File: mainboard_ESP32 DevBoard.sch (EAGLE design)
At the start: 41 parts, among them IC1 OP-AMP-2-LONG, IC2 OP-AMP-2-LONG, IC3 74HC08N, K1 AQH213, X1 JST-XH-02-PIN-LONG-PAD, X2 JST-XH-04-PIN-LONG-PAD, X3 1751248, X4 1751248, X5 JST-XH-04-PIN-LONG-PAD

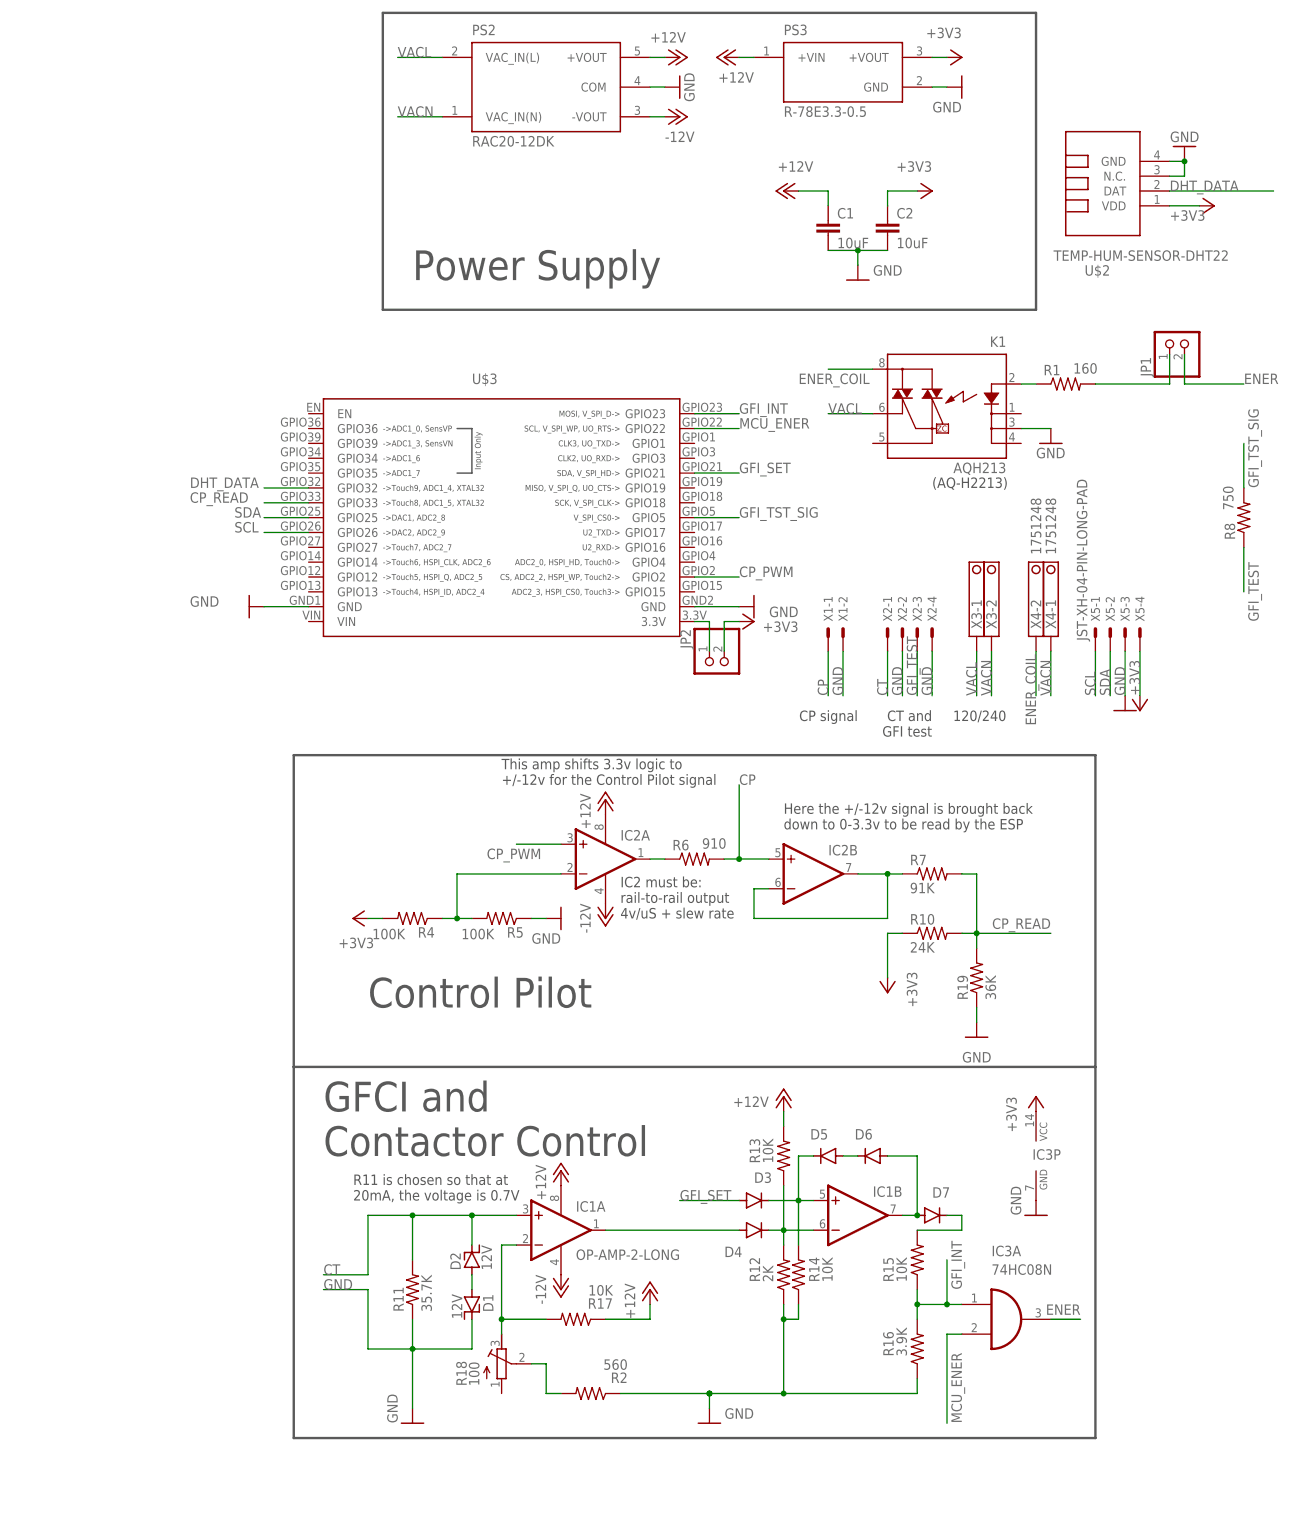
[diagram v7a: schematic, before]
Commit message: Added DG419 in place of op amp.
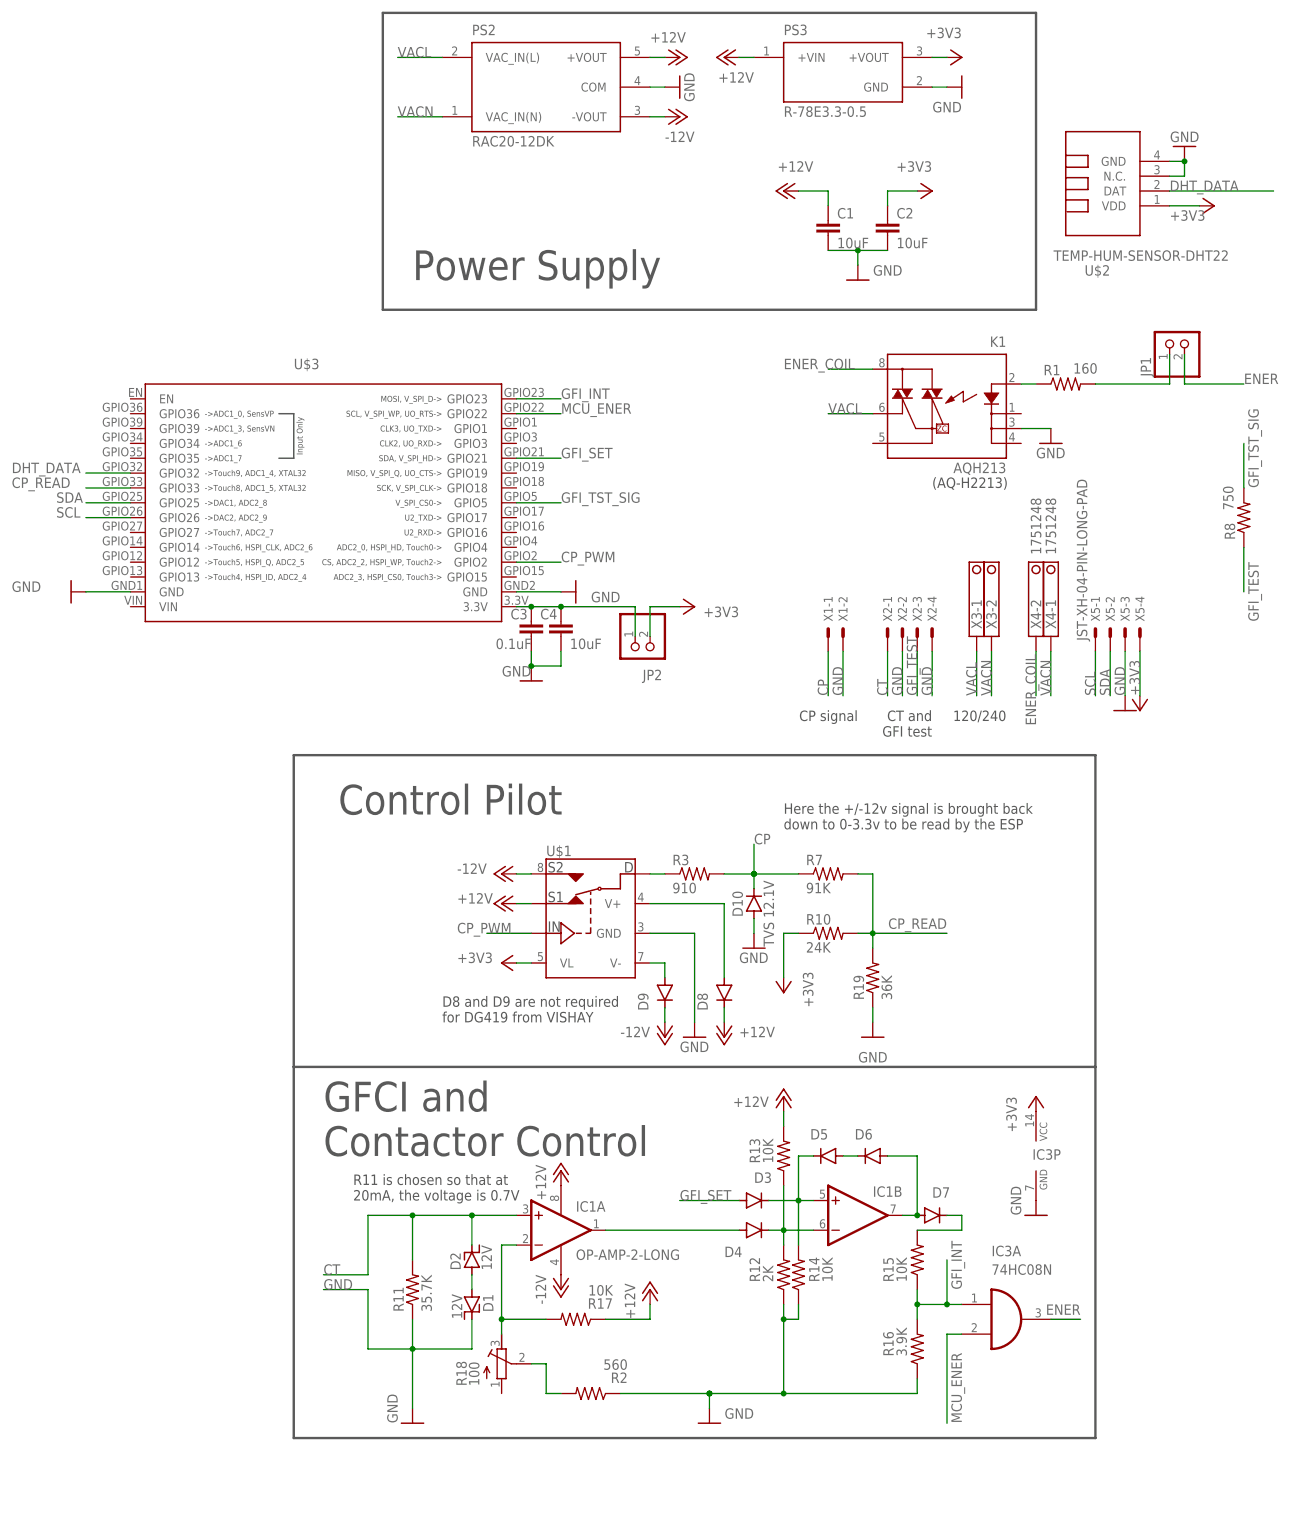
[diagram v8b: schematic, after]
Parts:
- removed IC2: OP-AMP-2-LONG, Op Amp:OP-AMP-2-LONG
- removed R4, R5: 100K, Passive:RESISTORL
- removed R6: 910, Passive:RESISTORL
- added C3: 0.1uF, rcl:C-EU025-025X050
- added C4: 10uF, rcl:C-EU025-025X050
- added D10: TVS 12.1V, Passive:DIODE
- added D8, D9: 1N4148DO35-7, diode:1N4148DO35-7
- added R3: 910, Passive:RESISTORL
- added U$1: DG419DJ-L, Analog Switches:DG419DJ-L
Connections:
- removed net N$16: IC2A.OUT, R6.1
- removed net N$17: IC2B.-IN, IC2B.OUT, R7.1
- new net N$11: D8.A, U$1.V+
- new net N$8: R3.1, U$1.D
- net +12V: now also D8.C, U$1.S1; no longer IC2P.V+
- net +3V3: now also U$1.VL; no longer R4.2
- net -12V: now also D9.C, U$1.S2; no longer IC2P.V-
- net CP: now also D10.C, R3.2, R7.1; no longer IC2B.+IN, R6.2
- net CP_PWM: now also U$1.IN; no longer IC2A.+IN
- net GND: now also C3.2, C4.2, D10.A, U$1.GND; no longer R5.1
- net N$10: now also C3.1, C4.1
- net N$15: now also D9.A, U$1.V-; no longer IC2A.-IN, R4.1, R5.2
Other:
- note added: "D8 and D9 are not required for DG419 from VISHAY"
- note removed: "IC2 must be: rail-to-rail output 4v/uS + slew rate"
- note removed: "This amp shifts 3.3v logic to +/-12v for the Control Pilot signal"
- moved on the sheet: JP2, R10, R19, R7, U$3
